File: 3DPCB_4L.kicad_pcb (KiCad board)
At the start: 4 copper layers, 100 x 60 mm, 846 parts, among them IC1 DRV8825, IC2 DRV8825, IC3 DRV8825, IC4 DRV8825, IC5 DRV8825, J1 SOLDER_JUMPER_3P, J10 , J11 , J12 , J13 , J14 , J15 , J16 , J2 , J3 , J4 , J5 , J6 , J7 , J8 , J9 , K1 CONN_3, K2 CONN_3, K3 CONN_3, K4 CONN_3, K5 CONN_3, K6 CONN_3, K7 CONN_3, K8 CONN_3, K9 CONN_3, P1 CONN_8, P10 CONN_2, P11 CONN_3X2, P12 CONN_3X2, P13 CONN_4, P2 CONN_2, P3 CONN_2, P4 CONN_2, P5 CONN_4, P6 CONN_4, P7 CONN_4, P8 CONN_2, P9 CONN_4, U1 CONN_4_LERCHE, U10 MICRO-SD, U11 TC4427, U12 MCP4728, U13 CONN_4_LERCHE, U15 SPST_MOMENTARY, U16 CONN_4_LERCHE, U17 TC4427, U2 SPST_MOMENTARY, U20 TPS6213X, U21 CONN_4_LERCHE, U22 CONN_4_LERCHE, U23 MCP4728, U24 MOS_NFET, U25 CONN_4_LERCHE, U3 BSS84, U4 CONN_4_LERCHE, U5 MOS_NFET, U6 LPC1768_TQFP100, U7 MOS_NFET, U8 MOS_NFET

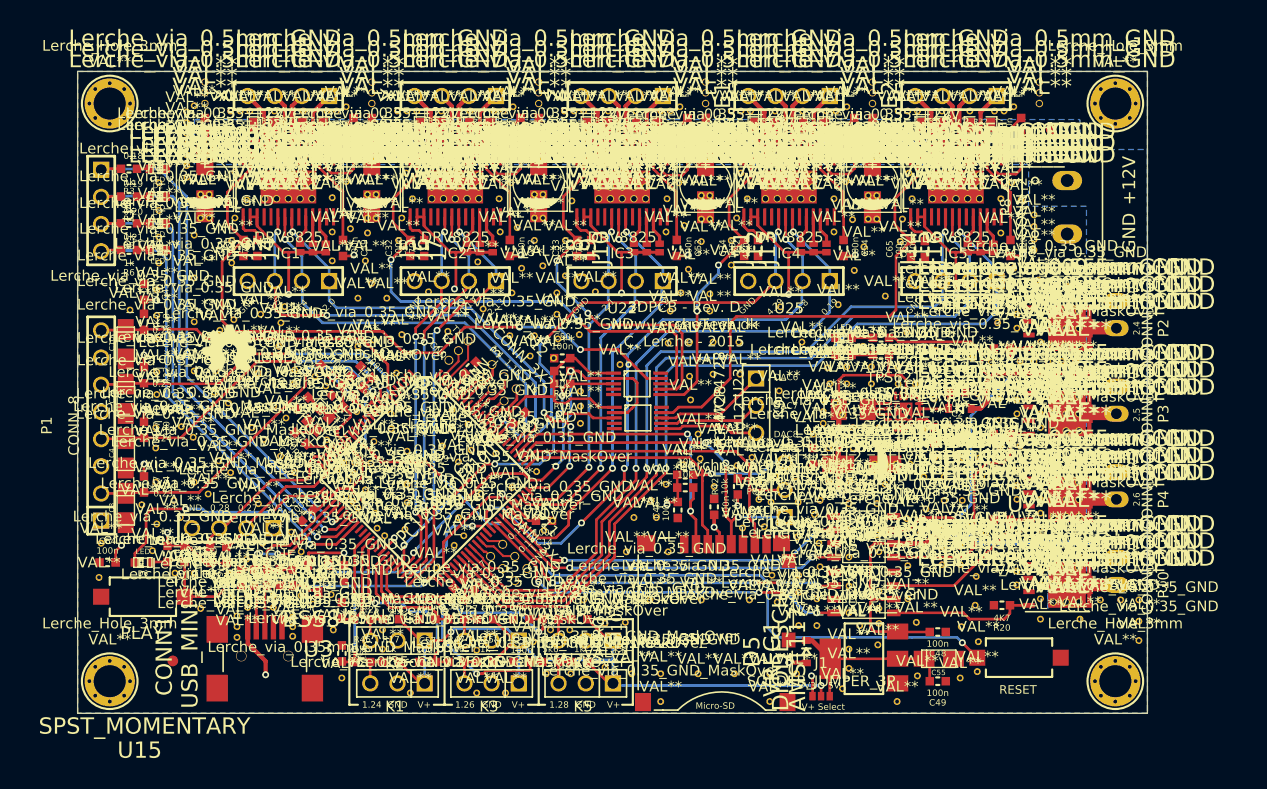
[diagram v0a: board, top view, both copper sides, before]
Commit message: PCB routed, needs specific BOM
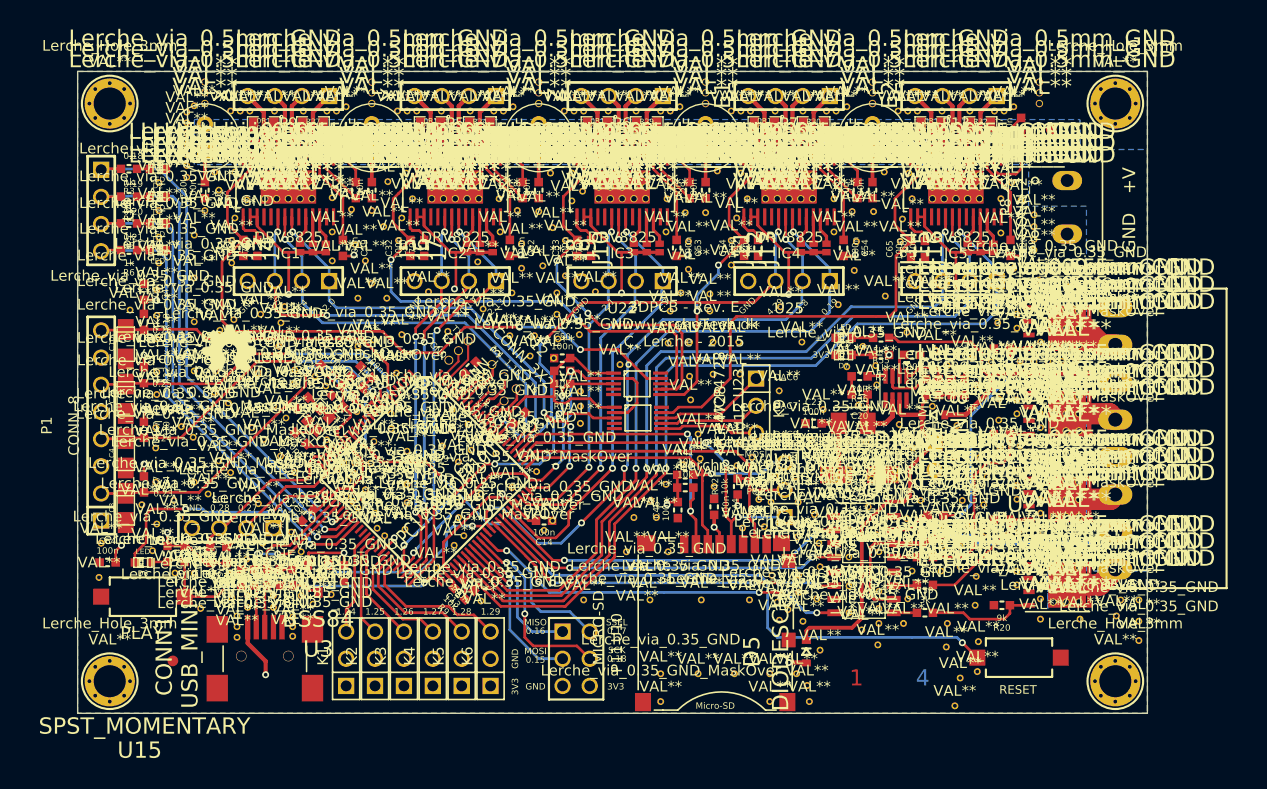
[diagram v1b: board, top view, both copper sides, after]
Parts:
- removed the ? at (200.8, 166.5)
- removed the ? at (157.9, 149.2)
- removed the ? at (157.1, 149.2)
- removed the ? at (200.1, 163.2)
- removed the ? at (173.5, 147.0)
- removed the ? at (199.4, 175.6)
- removed the ? at (201.8, 145.8)
- removed the ? at (186.2, 145.9)
- removed the ? at (188.3, 149.3)
- removed the ? at (189.1, 149.3)
- removed the ? at (203.9, 147.1)
- removed the ? at (199.7, 166.2)
- removed the ? at (199.7, 167.3)
- removed the ? at (199.7, 168.4)
- removed the ? at (202.5, 170.7)
- removed the ? at (205.5, 174.1)
- removed the ? at (205.5, 170.4)
- removed the ? at (170.5, 145.9)
- removed the ? at (204.7, 149.3)
- removed the ? at (209.3, 176.4)
- removed the ? at (172.7, 151.3)
- removed the ? at (201.5, 167.6)
- removed the ? at (204.7, 175.9)
- removed the ? at (141.5, 149.2)
- removed the ? at (142.3, 149.2)
- removed C47: 3.3nF, Lerche_C0603
- removed C48, C49, C56, C57, C58, C59, C60, C61: 100n, Lerche_C0603
- removed C55: 10uF, c_tant_A
- removed J1: SOLDER_JUMPER_3P, Lerche_Solder_Jumper_3P
- removed the Lerche_via_0.35_+12V at (141.5, 142.6)
- removed the Lerche_via_0.35_+12V at (173.5, 142.6)
- removed the Lerche_via_0.35_+12V at (172.7, 143.7)
- removed the Lerche_via_0.35_+12V at (173.5, 143.7)
- removed the Lerche_via_0.35_+12V at (188.3, 142.7)
- removed the Lerche_via_0.35_+12V at (189.1, 142.7)
- removed the Lerche_via_0.35_+12V at (188.3, 143.7)
- removed the Lerche_via_0.35_+12V at (189.1, 143.7)
- removed the Lerche_via_0.35_+12V at (203.9, 142.7)
- removed the Lerche_via_0.35_+12V at (204.7, 142.7)
- removed the Lerche_via_0.35_+12V at (203.9, 143.7)
- removed the Lerche_via_0.35_+12V at (142.3, 142.6)
- removed the Lerche_via_0.35_+12V at (204.7, 143.7)
- removed the Lerche_via_0.35_+12V at (141.5, 143.7)
- removed the Lerche_via_0.35_+12V at (142.3, 143.7)
- removed the Lerche_via_0.35_+12V at (157.1, 142.6)
- removed the Lerche_via_0.35_+12V at (157.9, 142.6)
- removed the Lerche_via_0.35_+12V at (157.1, 143.7)
- removed the Lerche_via_0.35_+12V at (157.9, 143.7)
- removed the Lerche_via_0.35_+12V at (172.7, 142.6)
- removed the Lerche_via_0.35_GND at (209.0, 169.0)
- removed the Lerche_via_0.35_GND at (200.2, 173.8)
- removed the Lerche_via_0.35_GND at (202.2, 173.8)
- removed the Lerche_via_0.35_GND at (202.1, 175.9)
- removed the Lerche_via_0.35_GND at (209.1, 173.4)
- removed the Lerche_via_0.35_GND at (207.8, 172.2)
- removed the Lerche_via_0.35_GND at (211.0, 175.6)
- removed the Lerche_via_0.35_GND at (210.1, 171.6)
- removed the Lerche_via_0.35_GND at (181.2, 187.0)
- removed the Lerche_via_0.35_GND at (212.7, 171.6)
- removed the Lerche_via_0.35_GND at (181.8, 191.8)
- removed the Lerche_via_0.35_GND at (211.0, 173.4)
- removed the Lerche_via_0.35_GND at (201.9, 164.7)
- removed the Lerche_via_0.35_GND at (204.2, 164.7)
- removed the Lerche_via_0.35_GND at (206.7, 164.7)
- removed the Lerche_via_0.35_GND at (204.9, 168.8)
- removed the Lerche_via_0.35_GND at (202.5, 168.8)
- removed the Lerche_via_0.35_GND at (204.5, 172.2)
- removed the Lerche_via_0.35_GND at (205.5, 172.2)
- removed the Lerche_via_0.35_GND at (206.5, 172.2)
- removed the Lerche_via_0.35_GND at (200.2, 170.7)
- removed the Lerche_via_0.35_GND at (200.3, 164.7)
- removed the Lerche_via_0.35_GND at (204.2, 163.1)
- removed the Lerche_via_0.35_GND at (206.7, 163.1)
- removed the Lerche_via_0.35_GND at (208.3, 164.7)
- removed the Lerche_via_0.35_GND at (211.4, 168.5)
- removed the Lerche_via_0.35_GND_MaskOver at (170.0, 193.6)
- removed the Lerche_via_0.35_GND_MaskOver at (167.3, 193.6)
- removed the Lerche_via_0.35_GND_MaskOver at (161.1, 193.6)
- removed the Lerche_via_0.35_GND_MaskOver at (153.9, 187.7)
- removed Lerche_via_0.35mm_GND_MaskOver (x11): VAL**, Lerche_via_0.35mm_GND_MaskOver
- removed P10, P3, P4: CONN_2, Lerche_2P_2.54mm_Large
- removed R17, R25, R26, R49, R50, R51: 1k, Lerche_R0603
- removed R46, R47, R48, R52, R53, R54: 5k6, Lerche_R0603
- removed U20: TPS6213X, Lerche_QFN16-EP
- removed VREG1: AMS1117, Lerche_SOT-223
- added ?: VAL**, Lerche_via_0.35_GND_MaskOver, F.Cu at (204.2, 172.8)
- added ?: VAL**, Lerche_via_0.35_GND_MaskOver, F.Cu at (205.3, 172.8)
- added ?: VAL**, Lerche_via_0.35_GND_MaskOver, F.Cu at (206.4, 172.8)
- added ?: VAL**, Lerche_via_0.35_GND_MaskOver, F.Cu at (206.4, 173.6)
- added ?: VAL**, Lerche_via_0.35_GND_MaskOver, F.Cu at (204.2, 173.6)
- added ?: VAL**, Lerche_via_0.35_GND_MaskOver, F.Cu at (205.3, 173.6)
- added ?: VAL**, Lerche_via_0.35_GND_MaskOver, F.Cu at (209.9, 166.8)
- added ?: VAL**, Lerche_via_0.35_GND_MaskOver, F.Cu at (206.8, 168.5)
- added ?: VAL**, Lerche_via_0.35_GND_MaskOver, F.Cu at (203.7, 170.1)
- added ?: VAL**, Lerche_via_0.35_GND_MaskOver, F.Cu at (202.0, 170.1)
- added ?: VAL**, Lerche_via_0.35_GND_MaskOver, F.Cu at (199.7, 167.1)
- added ?: VAL**, Lerche_via_0.35_GND_MaskOver, F.Cu at (203.0, 166.7)
- added ?: VAL**, Lerche_via_0.35_GND_MaskOver, F.Cu at (204.7, 164.8)
- added ?: VAL**, Lerche_via_0.35_GND_MaskOver, F.Cu at (204.6, 163.0)
- added ?: VAL**, Lerche_via_0.35_GND_MaskOver, F.Cu at (212.2, 168.6)
- added ?: VAL**, Lerche_via_0.35_GND_MaskOver, F.Cu at (214.0, 164.8)
- added ?: VAL**, Lerche_via_0.35_GND_MaskOver, F.Cu at (211.9, 171.5)
- added ?: VAL**, Lerche_via_0.35_GND_MaskOver, F.Cu at (208.1, 170.7)
- added ?: VAL**, Lerche_via_0.35_GND_MaskOver, F.Cu at (208.8, 175.6)
- added ?: VAL**, Lerche_via_0.35_GND_MaskOver, F.Cu at (203.9, 176.2)
- added ?: VAL**, Lerche_via_0.35_GND_MaskOver, F.Cu at (203.3, 187.7)
- added ?: VAL**, Lerche_via_0.35_GND_MaskOver, F.Cu at (214.7, 176.0)
- added ?: VAL**, Lerche_via_0.35_GND_MaskOver, F.Cu at (173.1, 148.6)
- added ?: VAL**, Lerche_via_0.35_GND_MaskOver, F.Cu at (177.2, 146.7)
- added ?: VAL**, Lerche_via_0.35_GND_MaskOver, F.Cu at (174.4, 150.1)
- added ?: VAL**, Lerche_via_0.35_GND_MaskOver, F.Cu at (143.2, 146.6)
- added C11: 100uF, C1V7, F.Cu at (210.1, 171.5)
- added C20: 100n, Lerche_C0603, F.Cu at (203.1, 165.7)
- added IC6: MP9943, Lerche_MP9943, F.Cu at (206.5, 165.1)
- added Lerche_via_0.35_+12V: VAL**, Lerche_via_0.35_+12V, F.Cu at (202.0, 172.8)
- added Lerche_via_0.35_+12V: VAL**, Lerche_via_0.35_+12V, F.Cu at (202.0, 173.6)
- added Lerche_via_0.35_+12V: VAL**, Lerche_via_0.35_+12V, F.Cu at (200.9, 173.6)
- added Lerche_via_0.35_+12V: VAL**, Lerche_via_0.35_+12V, F.Cu at (199.8, 173.6)
- added Lerche_via_0.35_+12V: VAL**, Lerche_via_0.35_+12V, F.Cu at (200.9, 172.8)
- added Lerche_via_0.35_+12V: VAL**, Lerche_via_0.35_+12V, F.Cu at (199.8, 172.8)
- added R35: 1M, Lerche_R0603, F.Cu at (209.3, 165.0)
- added R36: 20R, Lerche_R0603, F.Cu at (203.1, 164.0)
- added R38: 51k, Lerche_R0603, F.Cu at (210.5, 165.0)
- added R39: 13k, Lerche_R0603, F.Cu at (211.7, 165.0)
- added R40: 41k2, Lerche_R0603, F.Cu at (212.9, 165.0)
- added R56: 3k, Lerche_R0603, F.Cu at (210.2, 177.0)
- added R57: 3k, Lerche_R0603, F.Cu at (209.2, 183.5)
- added R58: 3k, Lerche_R0603, F.Cu at (209.2, 180.9)
- added R59: 3k, Lerche_R0603, F.Cu at (209.2, 186.1)
- C24, C25, C26, C27, C70: footprint c_elec_5x5.8 -> C1V7
- C43: value 100uF -> 47uF
- L2: value INDUCTOR -> IHLP1212-10uH
- P11: footprint Lerche_6P_1.6mm_2ROW -> pin_array_3x2
- P2: value CONN_2 -> CONN_8; footprint Lerche_2P_2.54mm_Large -> Lerche_8P_CONN_3,5mm
- R14, R15, R16, R20: value 4K7 -> 9k
- U11, U17: value TC4427 -> IX4427
- U24, U5, U7, U8: value MOS_NFET -> IRFH7932
- moved K5 11.8 mm to (165.9, 190.4), turned to 90 degrees
- moved P11 11.0 mm to (176.6, 190.4), turned to 270 degrees
- moved P2 10.3 mm to (227.0, 169.8), turned to 90 degrees
- moved K6 9.06 mm to (168.6, 190.4), turned to 90 degrees
- moved K3 8.52 mm to (160.5, 190.4), turned to 90 degrees
- moved C29 6.01 mm to (188.7, 146.6), turned to 90 degrees
- moved C38 6.01 mm to (202.9, 146.6)
- moved C36 6.00 mm to (171.6, 146.6)
- moved C37 6.00 mm to (187.2, 146.6)
- moved C8 6.00 mm to (156.0, 146.6)
- moved C28 6.00 mm to (173.1, 146.6), turned to 90 degrees
- moved C30 6.00 mm to (141.9, 146.6), turned to 90 degrees
- moved C31 6.00 mm to (157.5, 146.6), turned to 90 degrees
- moved C71 6.00 mm to (204.3, 146.6), turned to 90 degrees
- moved K4 5.76 mm to (163.2, 190.4), turned to 90 degrees
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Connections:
- net PWM0 renamed P2.4
- net PWM1 renamed P2.5
- C2 pad 1: N-00000208 -> N-0000071
- D5 pad 2: +5V -> VDCVDC
- D9 pad 2: N-00000208 -> VDCVDC
- K1 pad 1: N-00000197 -> +3.3V
- K2 pad 1: N-00000197 -> +3.3V
- K3 pad 1: N-00000197 -> +3.3V
- K4 pad 1: N-00000197 -> +3.3V
- K5 pad 1: N-00000197 -> +3.3V
- K6 pad 1: N-00000197 -> +3.3V
- P11 pad 1: SSEL1 -> MISO1
- P11 pad 2: MISO1 -> SSEL1
- P11 pad 3: SCK1 -> MOSI1
- P11 pad 4: MOSI1 -> SCK1
- P2 pad 1: +12V -> /P2.7_FET
- P2 pad 2: /PWM0_FET -> +12V
- R14 pad 1: N-00000138 -> N-0000095
- R15 pad 1: N-00000139 -> N-0000091
- R16 pad 1: N-00000137 -> N-0000086
- R20 pad 1: N-00000207 -> N-0000090
- U11 pad 5: N-00000207 -> N-0000088
- U11 pad 7: N-00000137 -> N-0000089
- U17 pad 5: N-00000139 -> N-0000087
- U17 pad 7: N-00000138 -> N-0000092
- U24 pad 1: N-00000207 -> N-0000090
- U5 pad 1: N-00000138 -> N-0000095
- U6 pad 38: X-MIN-LPC -> X-MIN
- U6 pad 39: X-MAX-LPC -> X-MAX
- U6 pad 40: Y-MIN-LPC -> Y-MIN
- U6 pad 43: Y-MAX-LPC -> Y-MAX
- U6 pad 44: Z-MIN-LPC -> Z-MIN
- U6 pad 45: Z-MAX-LPC -> Z-MAX
- U7 pad 1: N-00000139 -> N-0000091
- U8 pad 1: N-00000137 -> N-0000086
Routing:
- net N-00000197: track 71.1 -> 0.00 mm, vias 2 -> 0
- net VDCVDC: track 0.00 -> 35.2 mm
- net N-00000138: track 26.1 -> 0.00 mm, vias 2 -> 0
- net Z-MIN-LPC: track 24.2 -> 0.00 mm, vias 2 -> 0
- net N-00000139: track 22.5 -> 0.00 mm
- net Z-MAX-LPC: track 21.2 -> 0.00 mm, vias 2 -> 0
- net N-0000095: track 0.00 -> 20.9 mm, vias 0 -> 2
- net N-0000091: track 0.00 -> 18.9 mm
- net Y-MIN-LPC: track 17.8 -> 0.00 mm, vias 2 -> 0
- net +5V: track 17.6 -> 0.00 mm
- net +3.3V: track 189.4 -> 172.1 mm, vias 24 -> 22
- net N-00000137: track 15.7 -> 0.00 mm
- net SCK1: track 3.86 -> 18.1 mm, vias 0 -> 2
- net N-00000207: track 13.9 -> 0.00 mm
- net X-MIN-LPC: track 13.4 -> 0.00 mm, vias 2 -> 0
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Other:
- board text added: "+V"
- board text added: "1"
- board text added: "2"
- board text added: "3"
- board text added: "3DPCB - Rev. E www.LercheTech.dk C. Lerche - 2015"
- board text added: "4"
- board text added: "MISO"
- board text added: "MOSI"
- board text added: "SCK"
- board text added: "SCL"
- board text added: "SDA"
- board text added: "SSEL"
- board text added: "Three Dimensional Printer Controller Board (3DPCB) - Rev. E Smoothie-compatible - www.smoothieware.org"
- board text removed: "+12V"
- board text removed: "12V"
- board text removed: "3DPCB - Rev. D www.LercheTech.dk C. Lerche - 2015"
- board text removed: "5V"
- board text removed: "Three Dimensional Printer Controller Board (3DPCB) - Rev. C Smoothie-compatible - www.smoothieware.org"
- board text removed: "V+"
- board text removed: "V+ Select"

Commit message: All PCB is routed - PCB sent to production
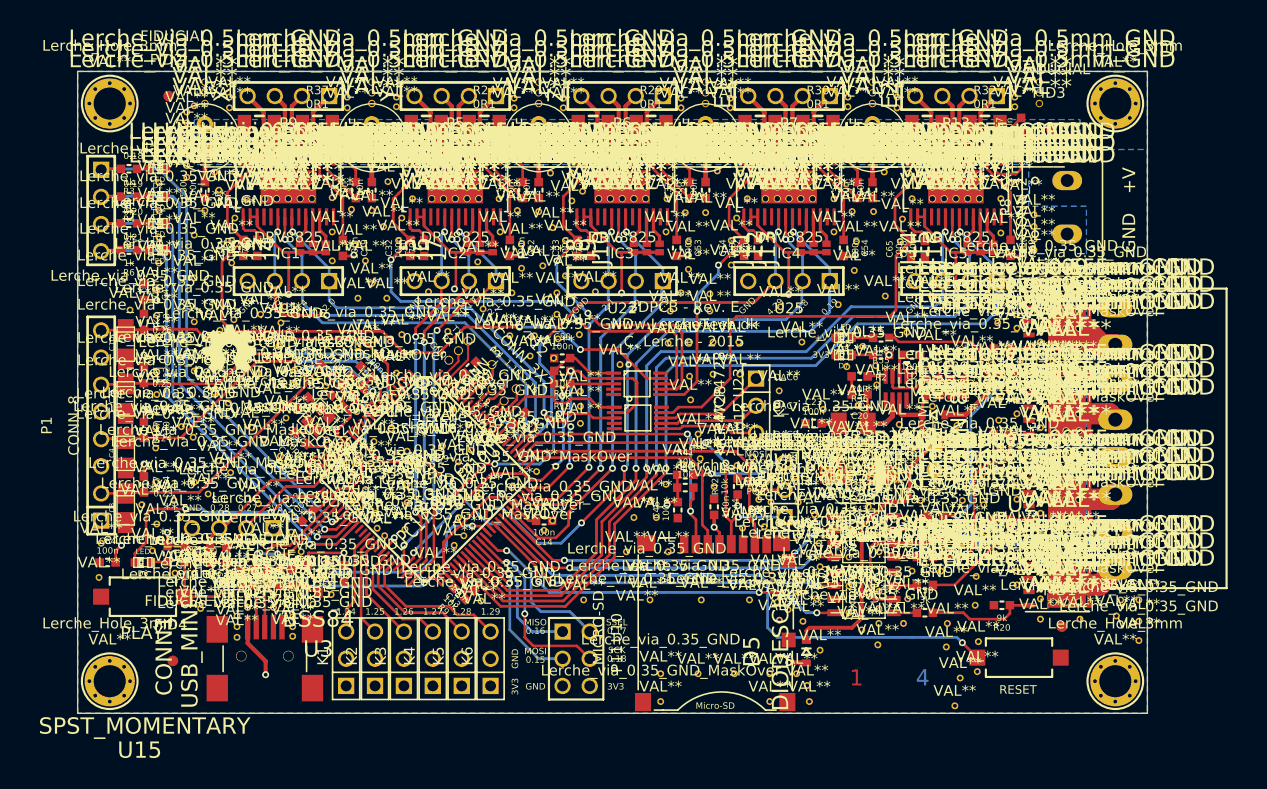
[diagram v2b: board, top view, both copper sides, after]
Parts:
- removed the ? at (144.3, 139.2)
- removed the ? at (155.1, 138.8)
- removed the ? at (159.9, 139.2)
- removed the ? at (170.7, 138.8)
- removed the ? at (175.5, 139.2)
- removed the ? at (186.3, 138.8)
- removed the ? at (191.1, 139.2)
- removed the ? at (201.9, 138.8)
- removed the ? at (206.7, 139.2)
- removed the ? at (217.5, 138.8)
- removed the ? at (138.9, 190.6)
- removed the ? at (221.0, 140.9)
- removed the ? at (216.6, 139.2)
- removed the ? at (213.4, 139.2)
- removed the ? at (210.8, 139.2)
- removed the ? at (208.5, 139.2)
- removed the ? at (197.8, 139.2)
- removed the ? at (195.2, 139.2)
- removed the ? at (182.2, 139.2)
- removed the ? at (179.6, 139.2)
- removed the ? at (166.7, 139.2)
- removed the ? at (164.0, 139.2)
- removed the ? at (151.1, 139.2)
- removed the ? at (148.4, 139.2)
- removed the ? at (200.0, 139.2)
- removed the ? at (200.9, 139.2)
- removed the ? at (192.9, 139.2)
- removed the ? at (192.0, 139.2)
- removed the ? at (215.7, 139.2)
- removed the ? at (207.6, 139.2)
- removed the ? at (184.5, 139.2)
- removed the ? at (185.4, 139.2)
- removed the ? at (177.3, 139.2)
- removed the ? at (176.4, 139.2)
- removed the ? at (168.9, 139.2)
- removed the ? at (169.8, 139.2)
- removed the ? at (161.7, 139.2)
- removed the ? at (160.8, 139.2)
- removed the ? at (153.3, 139.2)
- removed the ? at (154.2, 139.2)
- removed the ? at (146.1, 139.2)
- removed the ? at (145.2, 139.2)
- added ?: VAL**, Lerche_via_0.35mm_GND_MaskOver, F.Cu at (217.6, 137.9)
- added ?: VAL**, Lerche_via_0.35mm_GND_MaskOver, F.Cu at (217.6, 138.8)
- added ?: VAL**, Lerche_via_0.35mm_GND_MaskOver, F.Cu at (206.6, 137.9)
- added ?: VAL**, Lerche_via_0.35mm_GND_MaskOver, F.Cu at (206.6, 138.9)
- added ?: VAL**, Lerche_via_0.35mm_GND_MaskOver, F.Cu at (202.0, 138.8)
- added ?: VAL**, Lerche_via_0.35mm_GND_MaskOver, F.Cu at (202.0, 137.9)
- added ?: VAL**, Lerche_via_0.35mm_GND_MaskOver, F.Cu at (191.0, 138.9)
- added ?: VAL**, Lerche_via_0.35mm_GND_MaskOver, F.Cu at (191.0, 138.0)
- added ?: VAL**, Lerche_via_0.35mm_GND_MaskOver, F.Cu at (186.4, 138.0)
- added ?: VAL**, Lerche_via_0.35mm_GND_MaskOver, F.Cu at (186.4, 138.9)
- added ?: VAL**, Lerche_via_0.35mm_GND_MaskOver, F.Cu at (175.4, 138.9)
- added ?: VAL**, Lerche_via_0.35mm_GND_MaskOver, F.Cu at (175.4, 138.0)
- added ?: VAL**, Lerche_via_0.35mm_GND_MaskOver, F.Cu at (170.8, 138.9)
- added ?: VAL**, Lerche_via_0.35mm_GND_MaskOver, F.Cu at (170.8, 138.0)
- added ?: VAL**, Lerche_via_0.35mm_GND_MaskOver, F.Cu at (159.8, 138.8)
- added ?: VAL**, Lerche_via_0.35mm_GND_MaskOver, F.Cu at (159.8, 137.9)
- added ?: VAL**, Lerche_via_0.35mm_GND_MaskOver, F.Cu at (155.2, 138.9)
- added ?: VAL**, Lerche_via_0.35mm_GND_MaskOver, F.Cu at (155.2, 137.9)
- added ?: VAL**, Lerche_via_0.35mm_GND_MaskOver, F.Cu at (144.2, 138.9)
- added ?: VAL**, Lerche_via_0.35mm_GND_MaskOver, F.Cu at (144.2, 137.9)
- added FID1: FIDUCIAL, Lerche_Fiducial, F.Cu at (222.0, 187.4)
- added FID2: FIDUCIAL, Lerche_Fiducial, F.Cu at (138.5, 137.8)
- added FID3: FIDUCIAL, Lerche_Fiducial, F.Cu at (221.0, 140.9)
- added FID4: FIDUCIAL, Lerche_Fiducial, F.Cu at (138.9, 190.6)
- R21, R22, R23, R24, R29, R30, R31, R32, R33, R37: footprint SM0805 -> Lerche_R1206
- moved R29 0.41 mm to (183.6, 140.5)
- moved R31 0.41 mm to (209.4, 140.5)
- moved R21 0.41 mm to (162.6, 140.5)
- moved R22 0.41 mm to (178.2, 140.5)
- moved R23 0.41 mm to (193.8, 140.5)
- moved R24 0.41 mm to (168.0, 140.5)
- moved R30 0.41 mm to (199.2, 140.5)
- moved R32 0.41 mm to (214.8, 140.5)
- moved R33 0.41 mm to (147.0, 140.5)
- moved R37 0.41 mm to (152.4, 140.5)
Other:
- net class Default: clearance 0.16 -> 0.1524; trace_width 0.16 -> 0.1524
- rule trace_clearance: 0.16 -> 0.1524
- rule trace_min: 0.16 -> 0.1524

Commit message: All files added - Hardware is NOT tested yet
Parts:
- ? (x21): renamed from Lerche_via_0.5mm_GND; value VAL** -> (none)
- ?: value VAL** -> (none)
- moved ? 5.51 mm to (143.3, 182.8)
- renumbered G*** to ?, Lerche_via_0.5mm_GND to ?, Lerche_via_0.35_GND to ?, Lerche_via_0.35_+12V to ?, Lerche_via_0.35_GND_MaskOver to ?, Lerche_Hole_3mm to ?, FID1 to ?, FID2 to ?, FID3 to ?, FID4 to ?

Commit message: Changed placement of WEEE symbol, set layers visible
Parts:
- moved ? 5.46 mm to (140.7, 187.6)
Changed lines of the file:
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@@
     (links 1051)
     (no_connects 0)
-    (area 124.091727 131.3332 237.651491 200.0178)
+    (area 124.091727 131.3332 237.651491 199.527401)
     (thickness 1.6)
     (drawings 125)
@@
   (page A3)
   (layers
-    (15 F.Cu mixed hide)
+    (15 F.Cu mixed)
     (2 Inner2.Cu power hide)
     (1 Inner1.Cu power hide)
-    (0 B.Cu mixed hide)
+    (0 B.Cu mixed)
     (16 B.Adhes user)
     (17 F.Adhes user)
     (18 B.Paste user)
     (19 F.Paste user)
-    (20 B.SilkS user hide)
+    (20 B.SilkS user)
     (21 F.SilkS user)
     (22 B.Mask user)
@@
     (pad_to_mask_clearance 0)
     (aux_axis_origin 130 195.5)
-    (visible_elements 7FFF7CF7)
+    (visible_elements 7FFF7FFF)
     (pcbplotparams
       (layerselection 284196871)
@@
   )
   (module Logo_silk_WEEE_8x10mm (layer B.Cu)
-    (at 143.3 182.8)
+    (at 140.7 187.6)
     (descr "WEEE logo, 8x10mm")
     (attr smd)
